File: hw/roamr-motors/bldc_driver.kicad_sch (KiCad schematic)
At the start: 1 part, among them U1 DRV8316CRRGFR

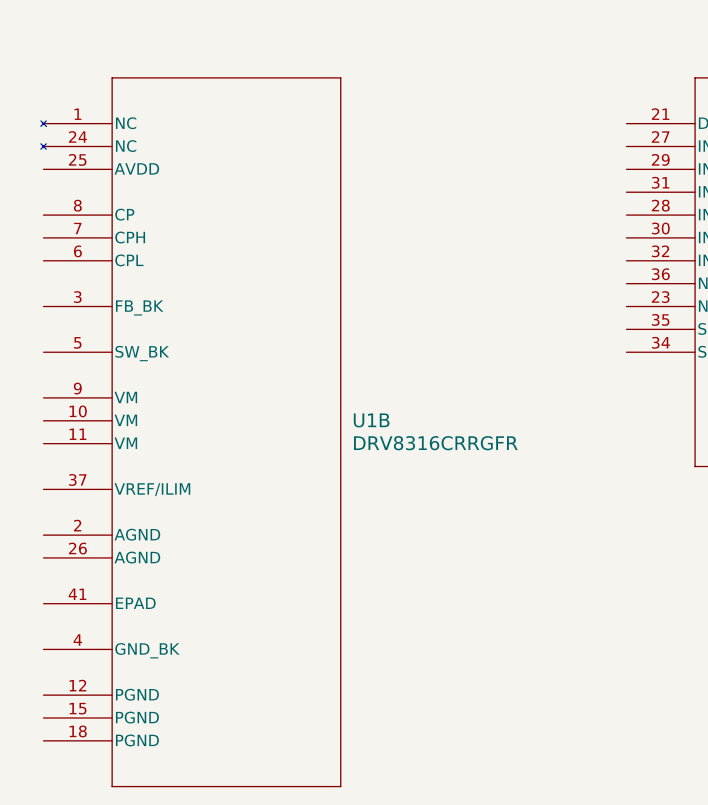
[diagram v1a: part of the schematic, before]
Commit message: Add USB-UART, USB receptacles, ESP32-S3-WROOM-1, switches. TODO: 5V_3V3 LDO, BLDC drivers, encoder SPI, connectors
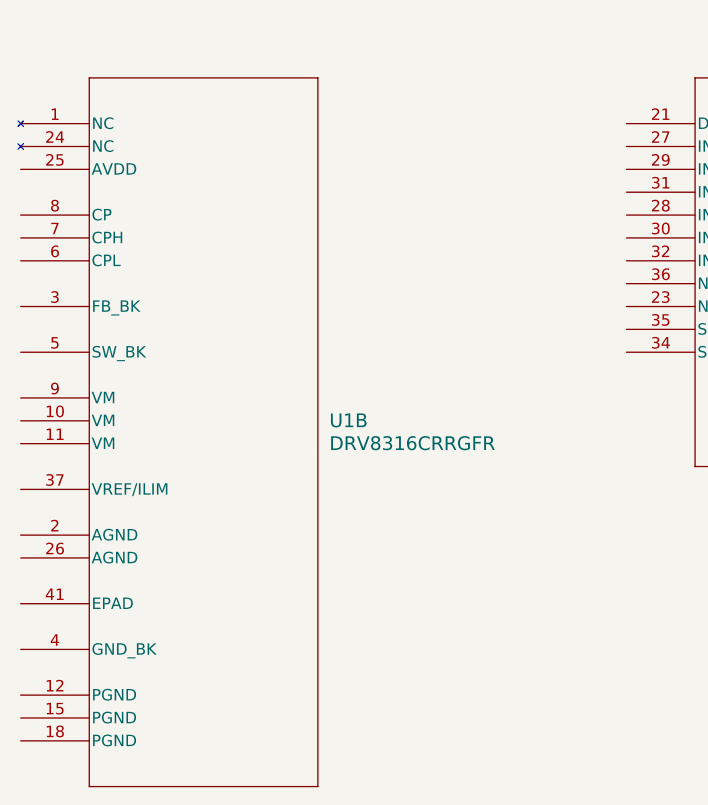
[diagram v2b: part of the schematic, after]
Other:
- moved on the sheet: U1B
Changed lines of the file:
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@@
 	(symbol
 		(lib_id "ul_DRV8316CRRGFR:DRV8316CRRGFR")
-		(at 64.77 60.96 0)
+		(at 62.23 60.96 0)
 		(unit 2)
 		(exclude_from_sim no)
@@
 		(fields_autoplaced yes)
 		(property "Reference" "U1"
-			(at 99.06 93.9799 0)
+			(at 96.52 93.9799 0)
 			(effects
 				(font
@@
 		)
 		(property "Value" "DRV8316CRRGFR"
-			(at 99.06 96.5199 0)
+			(at 96.52 96.5199 0)
 			(effects
 				(font
@@
 		)
 		(property "Footprint" "VQFN40_RGF_TEX"
-			(at 64.77 60.96 0)
+			(at 62.23 60.96 0)
 			(effects
 				(font
@@
 		)
 		(property "Datasheet" "https://www.ti.com/lit/gpn/drv8316c"
-			(at 64.77 60.96 0)
+			(at 62.23 60.96 0)
 			(effects
 				(font
@@
 		)
 		(property "Description" ""
-			(at 64.77 60.96 0)
+			(at 62.23 60.96 0)
 			(effects
 				(font

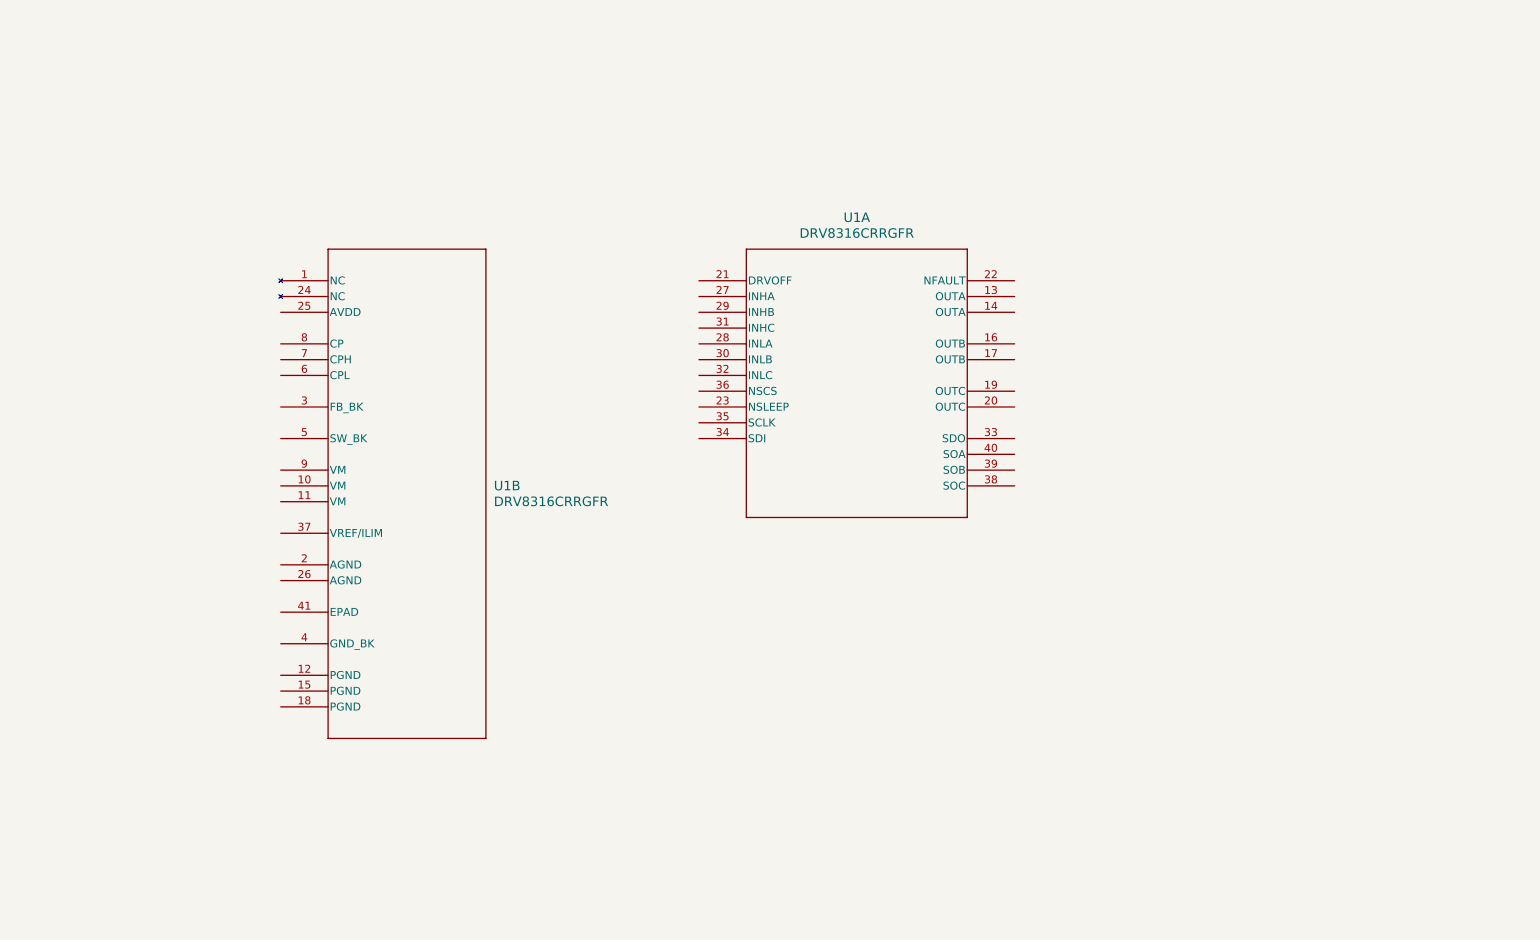
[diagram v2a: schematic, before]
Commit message: finished schematic and assigning most footprints
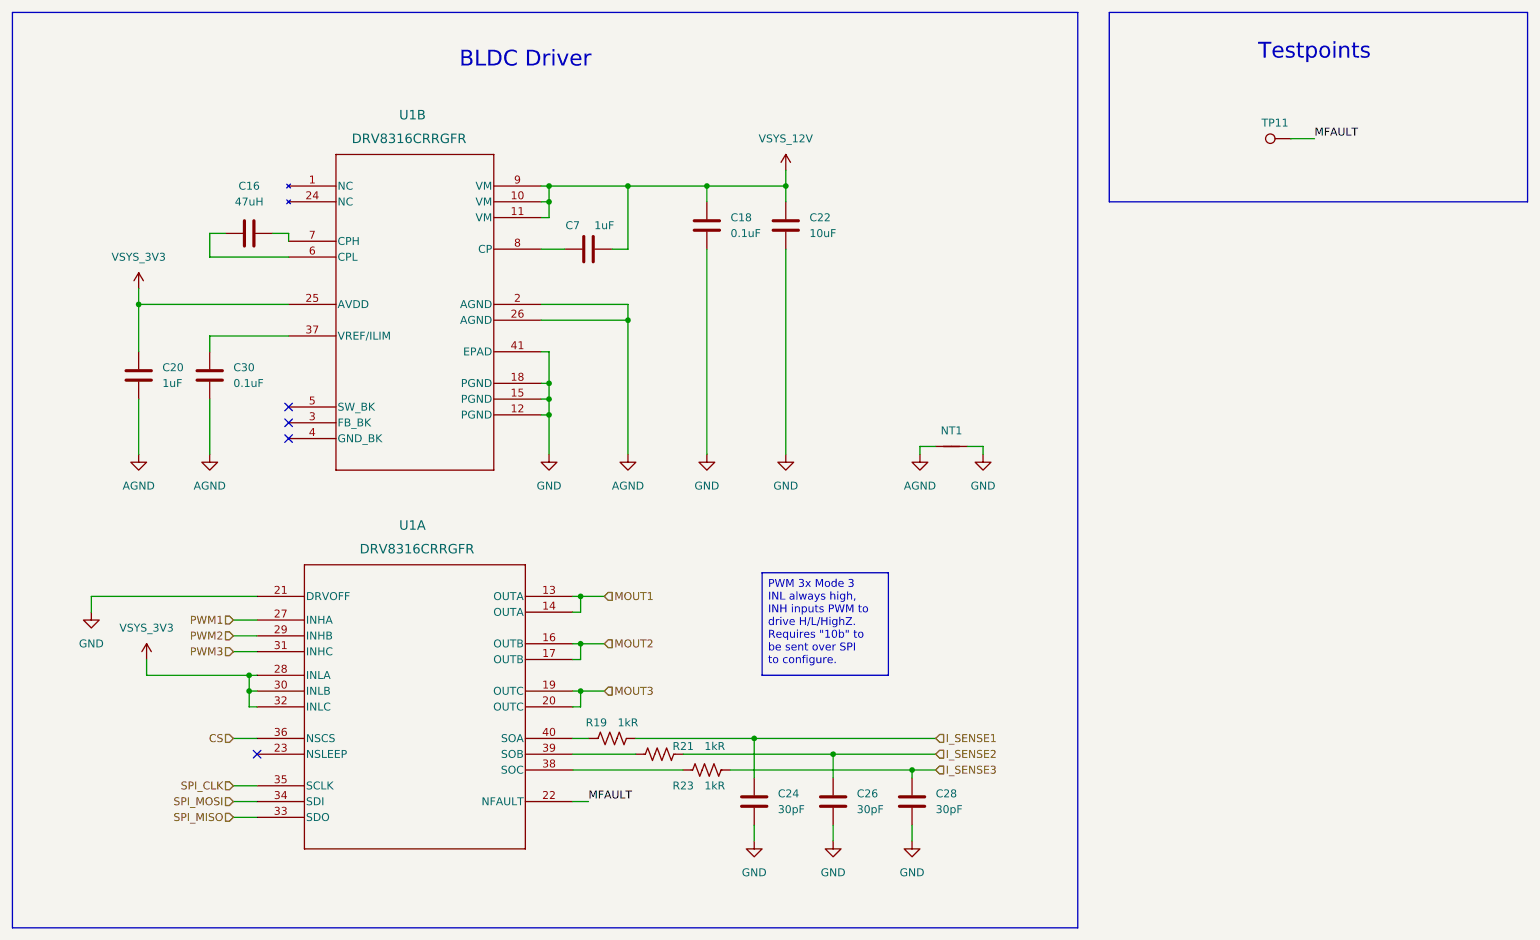
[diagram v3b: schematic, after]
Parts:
- added C16: 47uH, Capacitor_SMD:C_0603_1608Metric, symbol Device:C
- added C18, C30: 0.1uF, Capacitor_SMD:C_0603_1608Metric, symbol Device:C
- added C20, C7: 1uF, Capacitor_SMD:C_0603_1608Metric, symbol Device:C
- added C22: 10uF, Capacitor_SMD:C_0603_1608Metric, symbol Device:C
- added C24, C26, C28: 30pF, Capacitor_SMD:C_0603_1608Metric, symbol Device:C
- added NT1: NetTie_2, NetTie:NetTie-2_SMD_Pad0.5mm, symbol Device:NetTie_2
- added R19, R21, R23: 1kR, Resistor_SMD:R_0603_1608Metric, symbol Device:R_US
- added TP11: TestPoint, TestPoint:TestPoint_Pad_D1.5mm, symbol Connector:TestPoint
- U1: footprint VQFN40_RGF_TEX -> DRV8316CRRGFR:VQFN40_RGF_TEX
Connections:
- net MOUT1: now reaches U1.13 (OUTA)
- net MOUT1: now also U1.14 (OUTA)
- net MOUT2: now reaches U1.16 (OUTB)
- net MOUT2: now also U1.17 (OUTB)
- net MOUT3: now reaches U1.19 (OUTC)
- net MOUT3: now also U1.20 (OUTC)
- net GND: now reaches U1.21 (DRVOFF)
- net GND: now also U1.12 (PGND), U1.15 (PGND), U1.18 (PGND), U1.41 (EPAD), C18.2, C22.2, C24.2, C26.2, C28.2, NT1.2
- net MFAULT: now reaches U1.22 (NFAULT)
- net MFAULT: now also TP11.1
- net PWM1: now reaches U1.27 (INHA)
- net VSYS_3V3: now reaches U1.28 (INLA)
- net VSYS_3V3: now also U1.25 (AVDD), U1.30 (INLB), U1.32 (INLC), C20.1
- net PWM2: now reaches U1.29 (INHB)
- net PWM3: now reaches U1.31 (INHC)
- net SPI_MISO: now reaches U1.33 (SDO)
- net SPI_MOSI: now reaches U1.34 (SDI)
- net SPI_CLK: now reaches U1.35 (SCLK)
- net CS: now reaches U1.36 (NSCS)
- net at U1.38 (SOC): now also R23.1
- net at U1.39 (SOB): now also R21.1
- net at U1.40 (SOA): now also R19.1
- net VSYS_12V: now reaches U1.10 (VM)
- net VSYS_12V: now also U1.11 (VM), U1.9 (VM), C18.1, C22.1, C7.2
- net AGND: now reaches U1.2 (AGND)
- net AGND: now also U1.26 (AGND), C20.2, C30.2, NT1.1
- net at U1.37 (VREF/ILIM): now also C30.1
- net at U1.6 (CPL): now also C16.1
- net at U1.7 (CPH): now also C16.2
- net at U1.8 (CP): now also C7.1
- new net I_SENSE1: C24.1, R19.2
- new net I_SENSE2: C26.1, R21.2
- new net I_SENSE3: C28.1, R23.2
- no-connect marks 0 -> 4
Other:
- note added: "BLDC Driver"
- note added: "Testpoints"
- company: (none) -> Mechatronics FYDP Group 16
- moved on the sheet: U1A, U1B

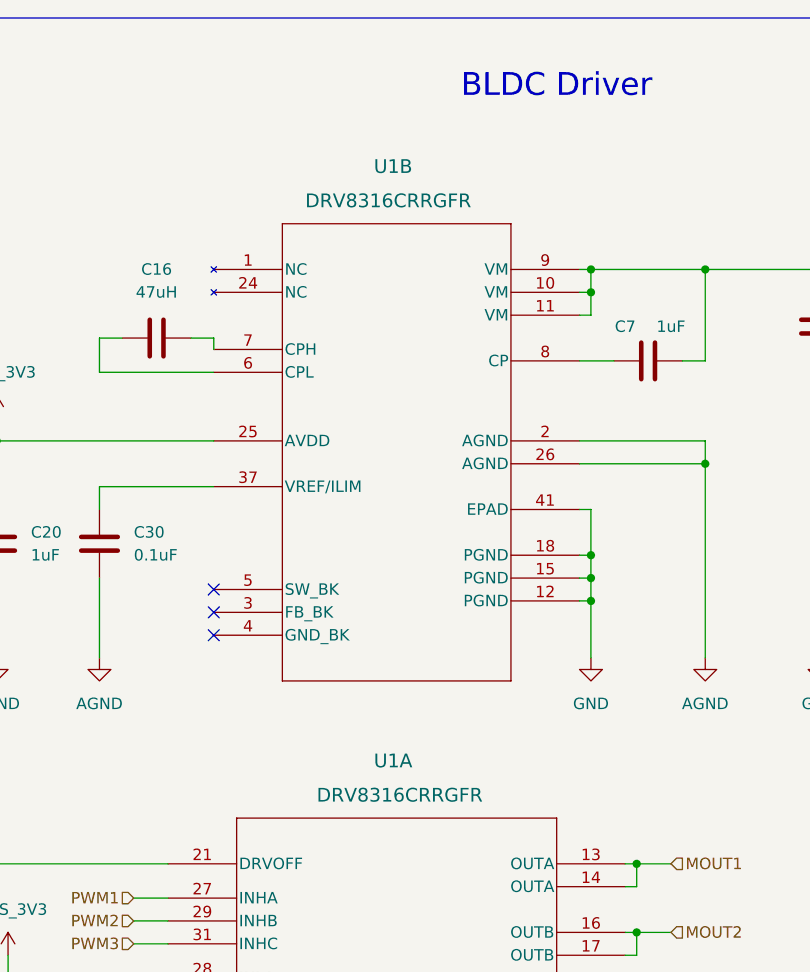
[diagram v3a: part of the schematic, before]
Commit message: added all footprints, starting layout properly
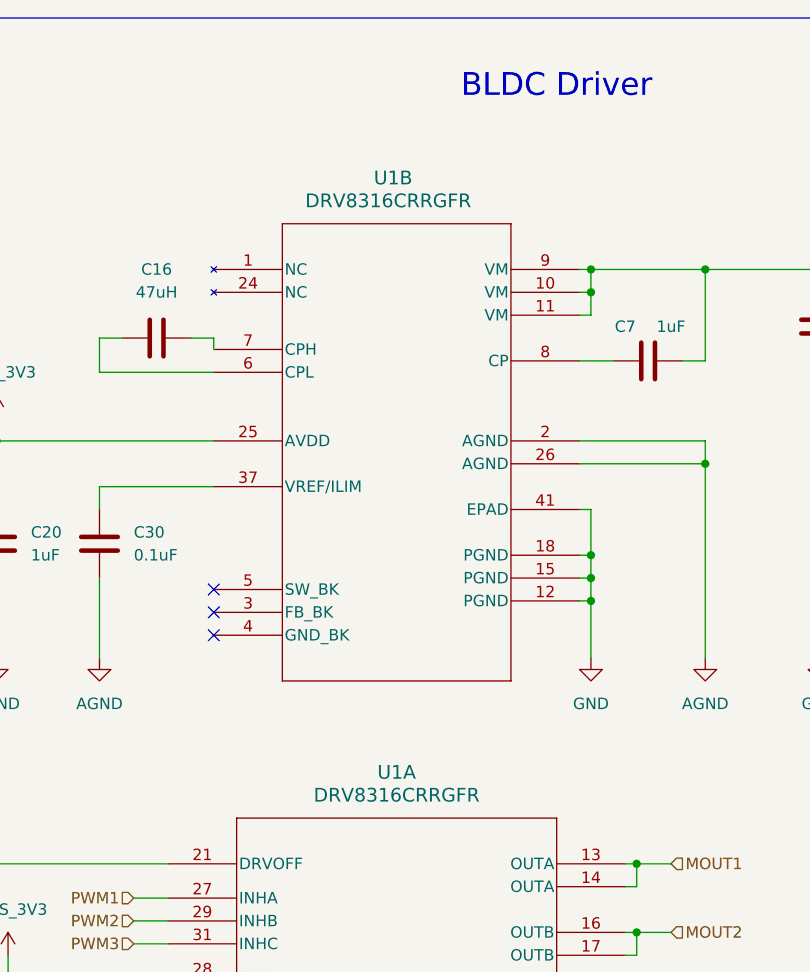
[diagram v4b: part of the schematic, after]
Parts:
- removed U1: DRV8316CRRGFR, DRV8316CRRGFR:VQFN40_RGF_TEX, symbol ul_DRV8316CRRGFR:DRV8316CRRGFR
- added U1: DRV8316CRRGFR, DRV8316CRRGFR:VQFN40_RGF_TEX, symbol DRV8316CRRGFR:DRV8316CRRGFR
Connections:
- net AGND: now also U1.2 (AGND), U1.26 (AGND)
- net CS: now also U1.36 (NSCS)
- net GND: now also U1.12 (PGND), U1.15 (PGND), U1.18 (PGND), U1.21 (DRVOFF), U1.41 (EPAD)
- net MFAULT: now also U1.22 (NFAULT)
- net MOUT1: now also U1.13 (OUTA), U1.14 (OUTA)
- net MOUT2: now also U1.16 (OUTB), U1.17 (OUTB)
- net MOUT3: now also U1.19 (OUTC), U1.20 (OUTC)
- net PWM1: now also U1.27 (INHA)
- net PWM2: now also U1.29 (INHB)
- net PWM3: now also U1.31 (INHC)
- net SPI_CLK: now also U1.35 (SCLK)
- net SPI_MISO: now also U1.33 (SDO)
- net SPI_MOSI: now also U1.34 (SDI)
- net VSYS_12V: now also U1.10 (VM), U1.11 (VM), U1.9 (VM)
- net VSYS_3V3: now also U1.25 (AVDD), U1.28 (INLA), U1.30 (INLB), U1.32 (INLC)
- net at C16.1: now also U1.6 (CPL)
- net at C16.2: now also U1.7 (CPH)
- net at R23.1: now also U1.38 (SOC)
- net at R21.1: now also U1.39 (SOB)
- net at R19.1: now also U1.40 (SOA)
- net at C30.1: now also U1.37 (VREF/ILIM)
- net at C7.1: now also U1.8 (CP)
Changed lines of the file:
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@@
 	)
 	(symbol
-		(lib_id "ul_DRV8316CRRGFR:DRV8316CRRGFR")
-		(at 58.42 111.76 0)
-		(unit 1)
+		(lib_name "DRV8316CRRGFR_1")
+		(lib_id "DRV8316CRRGFR:DRV8316CRRGFR")
+		(at 63.5 45.72 0)
+		(unit 2)
 		(exclude_from_sim no)
 		(in_bom yes)
@@
 		(dnp no)
 		(property "Reference" "U1"
-			(at 81.28 100.33 0)
+			(at 81.28 35.56 0)
 			(effects
 				(font
@@
 		)
 		(property "Value" "DRV8316CRRGFR"
-			(at 74.93 104.14 0)
+			(at 73.66 38.1 0)
 			(effects
 				(font
@@
 		)
 		(property "Footprint" "DRV8316CRRGFR:VQFN40_RGF_TEX"
-			(at 58.42 113.03 0)
+			(at 63.5 45.72 0)
 			(effects
 				(font
@@
 		)
 		(property "Datasheet" "https://www.ti.com/lit/gpn/drv8316c"
-			(at 58.42 113.03 0)
+			(at 63.5 45.72 0)
 			(effects
 				(font
@@
 		)
 		(property "Description" ""
-			(at 58.42 111.76 0)
-			(effects
-				(font
-					(size 1.27 1.27)
-				)
-				(hide yes)
-			)
+			(at 63.5 45.72 0)
+			(effects
+				(font
+					(size 1.27 1.27)
+				)
+				(hide yes)
+			)
+		)
+		(pin "34"
+		)
+		(pin "38"
+		)
+		(pin "39"
+		)
+		(pin "40"
+		)
+		(pin "35"
+		)
+		(pin "18"
+		)
+		(pin "33"
+		)
+		(pin "20"
+		)
+		(pin "23"
+		)
+		(pin "37"
+		)
+		(pin "36"
+		)
+		(pin "6"
+		)
+		(pin "3"
+		)
+		(pin "31"
+		)
+		(pin "32"
+		)
+		(pin "29"
+		)
+		(pin "15"
+		)
+		(pin "30"
+		)
+		(pin "5"
+		)
+		(pin "41"
+		)
+		(pin "11"
+		)
+		(pin "17"
+		)
+		(pin "7"
+		)
+		(pin "27"
 		)
 		(pin "22"
 		)
-		(pin "23"
-		)
-		(pin "30"
-		)
-		(pin "17"
+		(pin "21"
+		)
+		(pin "13"
+		)
+		(pin "14"
+		)
+		(pin "1"
+		)
+		(pin "2"
+		)
+		(pin "16"
+		)
+		(pin "26"
+		)
+		(pin "8"
+		)
+		(pin "9"
+		)
+		(pin "24"
+		)
+		(pin "25"
+		)
+		(pin "12"
 		)
 		(pin "19"
 		)
-		(pin "35"
-		)
-		(pin "14"
-		)
-		(pin "32"
-		)
-		(pin "29"
-		)
-		(pin "36"
-		)
-		(pin "34"
-		)
-		(pin "16"
-		)
-		(pin "27"
-		)
-		(pin "40"
-		)
-		(pin "13"
-		)
-		(pin "20"
-		)
-		(pin "33"
+		(pin "4"
 		)
 		(pin "28"
 		)
-		(pin "31"
-		)
-		(pin "21"
-		)
-		(pin "39"
-		)
-		(pin "38"
-		)
-		(pin "1"
-		)
-		(pin "24"
-		)
-		(pin "25"
-		)
-		(pin "8"
-		)
-		(pin "7"
-		)
-		(pin "6"
-		)
-		(pin "3"
-		)
-		(pin "5"
-		)
-		(pin "9"
-		)
 		(pin "10"
 		)
-		(pin "11"
-		)
-		(pin "37"
-		)
-		(pin "2"
-		)
-		(pin "26"
-		)
-		(pin "41"
-		)
-		(pin "4"
-		)
-		(pin "12"
-		)
-		(pin "15"
-		)
-		(pin "18"
-		)
 		(instances
 			(project ""
 				(path "/db664d1d-d972-4e66-af85-94b6971e1c6e/6fb3ef19-f3df-431d-bde7-764fb42db7f0"
 					(reference "U2")
-					(unit 1)
+					(unit 2)
 				)
 				(path "/db664d1d-d972-4e66-af85-94b6971e1c6e/c69cc801-0c40-4712-a8df-c9e7b1a11d6f"
 					(reference "U1")
-					(unit 1)
+					(unit 2)
 				)
 			)
@@
 	)
 	(symbol
-		(lib_name "DRV8316CRRGFR_1")
-		(lib_id "ul_DRV8316CRRGFR:DRV8316CRRGFR")
-		(at 63.5 45.72 0)
-		(unit 2)
-		(exclude_from_sim no)
-		(in_bom yes)
-		(on_board yes)
-		(dnp no)
+		(lib_id "DRV8316CRRGFR:DRV8316CRRGFR")
+		(at 58.42 111.76 0)
+		(unit 1)
+		(exclude_from_sim no)
+		(in_bom yes)
+		(on_board yes)
+		(dnp no)
+		(fields_autoplaced yes)
 		(property "Reference" "U1"
-			(at 81.28 34.29 0)
+			(at 83.82 101.6 0)
 			(effects
 				(font
 					(size 1.524 1.524)
 				)
-				(justify left)
 			)
 		)
 		(property "Value" "DRV8316CRRGFR"
-			(at 73.66 38.1 0)
+			(at 83.82 104.14 0)
 			(effects
 				(font
 					(size 1.524 1.524)
 				)
-				(justify left)
 			)
 		)
 		(property "Footprint" "DRV8316CRRGFR:VQFN40_RGF_TEX"
-			(at 63.5 46.99 0)
+			(at 58.42 111.76 0)
 			(effects
 				(font
@@
 		)
 		(property "Datasheet" "https://www.ti.com/lit/gpn/drv8316c"
-			(at 63.5 46.99 0)
+			(at 58.42 111.76 0)
 			(effects
 				(font
@@
 		)
 		(property "Description" ""
-			(at 63.5 45.72 0)
-			(effects
-				(font
-					(size 1.27 1.27)
-				)
-				(hide yes)
-			)
+			(at 58.42 111.76 0)
+			(effects
+				(font
+					(size 1.27 1.27)
+				)
+				(hide yes)
+			)
+		)
+		(pin "34"
+		)
+		(pin "38"
+		)
+		(pin "39"
+		)
+		(pin "40"
+		)
+		(pin "35"
+		)
+		(pin "18"
+		)
+		(pin "33"
+		)
+		(pin "20"
+		)
+		(pin "23"
+		)
+		(pin "37"
+		)
+		(pin "36"
+		)
+		(pin "6"
+		)
+		(pin "3"
+		)
+		(pin "31"
+		)
+		(pin "32"
+		)
+		(pin "29"
+		)
+		(pin "15"
+		)
+		(pin "30"
+		)
+		(pin "5"
+		)
+		(pin "41"
+		)
+		(pin "11"
+		)
+		(pin "17"
+		)
+		(pin "7"
+		)
+		(pin "27"
 		)
 		(pin "22"
 		)
-		(pin "23"
-		)
-		(pin "30"
-		)
-		(pin "17"
+		(pin "21"
+		)
+		(pin "13"
+		)
+		(pin "14"
+		)
+		(pin "1"
+		)
+		(pin "2"
+		)
+		(pin "16"
+		)
+		(pin "26"
+		)
+		(pin "8"
+		)
+		(pin "9"
+		)
+		(pin "24"
+		)
+		(pin "25"
+		)
+		(pin "12"
 		)
 		(pin "19"
 		)
-		(pin "35"
-		)
-		(pin "14"
-		)
-		(pin "32"
-		)
-		(pin "29"
-		)
-		(pin "36"
-		)
-		(pin "34"
-		)
-		(pin "16"
-		)
-		(pin "27"
-		)
-		(pin "40"
-		)
-		(pin "13"
-		)
-		(pin "20"
-		)
-		(pin "33"
+		(pin "4"
 		)
 		(pin "28"
 		)
-		(pin "31"
-		)
-		(pin "21"
-		)
-		(pin "39"
-		)
-		(pin "38"
-		)
-		(pin "1"
-		)
-		(pin "24"
-		)
-		(pin "25"
-		)
-		(pin "8"
-		)
-		(pin "7"
-		)
-		(pin "6"
-		)
-		(pin "3"
-		)
-		(pin "5"
-		)
-		(pin "9"
-		)
 		(pin "10"
 		)
-		(pin "11"
-		)
-		(pin "37"
-		)
-		(pin "2"
-		)
-		(pin "26"
-		)
-		(pin "41"
-		)
-		(pin "4"
-		)
-		(pin "12"
-		)
-		(pin "15"
-		)
-		(pin "18"
-		)
 		(instances
 			(project ""
 				(path "/db664d1d-d972-4e66-af85-94b6971e1c6e/6fb3ef19-f3df-431d-bde7-764fb42db7f0"
 					(reference "U2")
-					(unit 2)
+					(unit 1)
 				)
 				(path "/db664d1d-d972-4e66-af85-94b6971e1c6e/c69cc801-0c40-4712-a8df-c9e7b1a11d6f"
 					(reference "U1")
-					(unit 2)
-				)
-			)
+					(unit 1)
+				)
+			)

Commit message: more layout, i think i get do it on one side
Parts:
- removed C22: 10uF, Capacitor_SMD:C_0603_1608Metric, symbol Device:C
- added C19: 10uF, RVT1E100M0405:RVT1E100M0405, symbol Device:C_Polarized
- C15: renamed from C16; value 47uH -> 47uF
- renumbered C20 to C13, C30 to C14, C7 to C16, C18 to C17, C24 to C18, C26 to C20, C28 to C21, R19 to R20, R23 to R22, U1 to U4
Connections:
- net AGND: now also C18.2, C20.2, C21.2
- net GND: now also C19.2; no longer C18.2, C20.2, C21.2
- net VSYS_12V: now also C19.1

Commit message: layout done except i need to add two fuses
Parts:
- removed NT1: NetTie_2, NetTie:NetTie-2_SMD_Pad0.5mm, symbol Device:NetTie_2
